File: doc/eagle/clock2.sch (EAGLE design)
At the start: 27 parts, among them J1 LCD 1602, J2 LM35, J3 ds1302 module

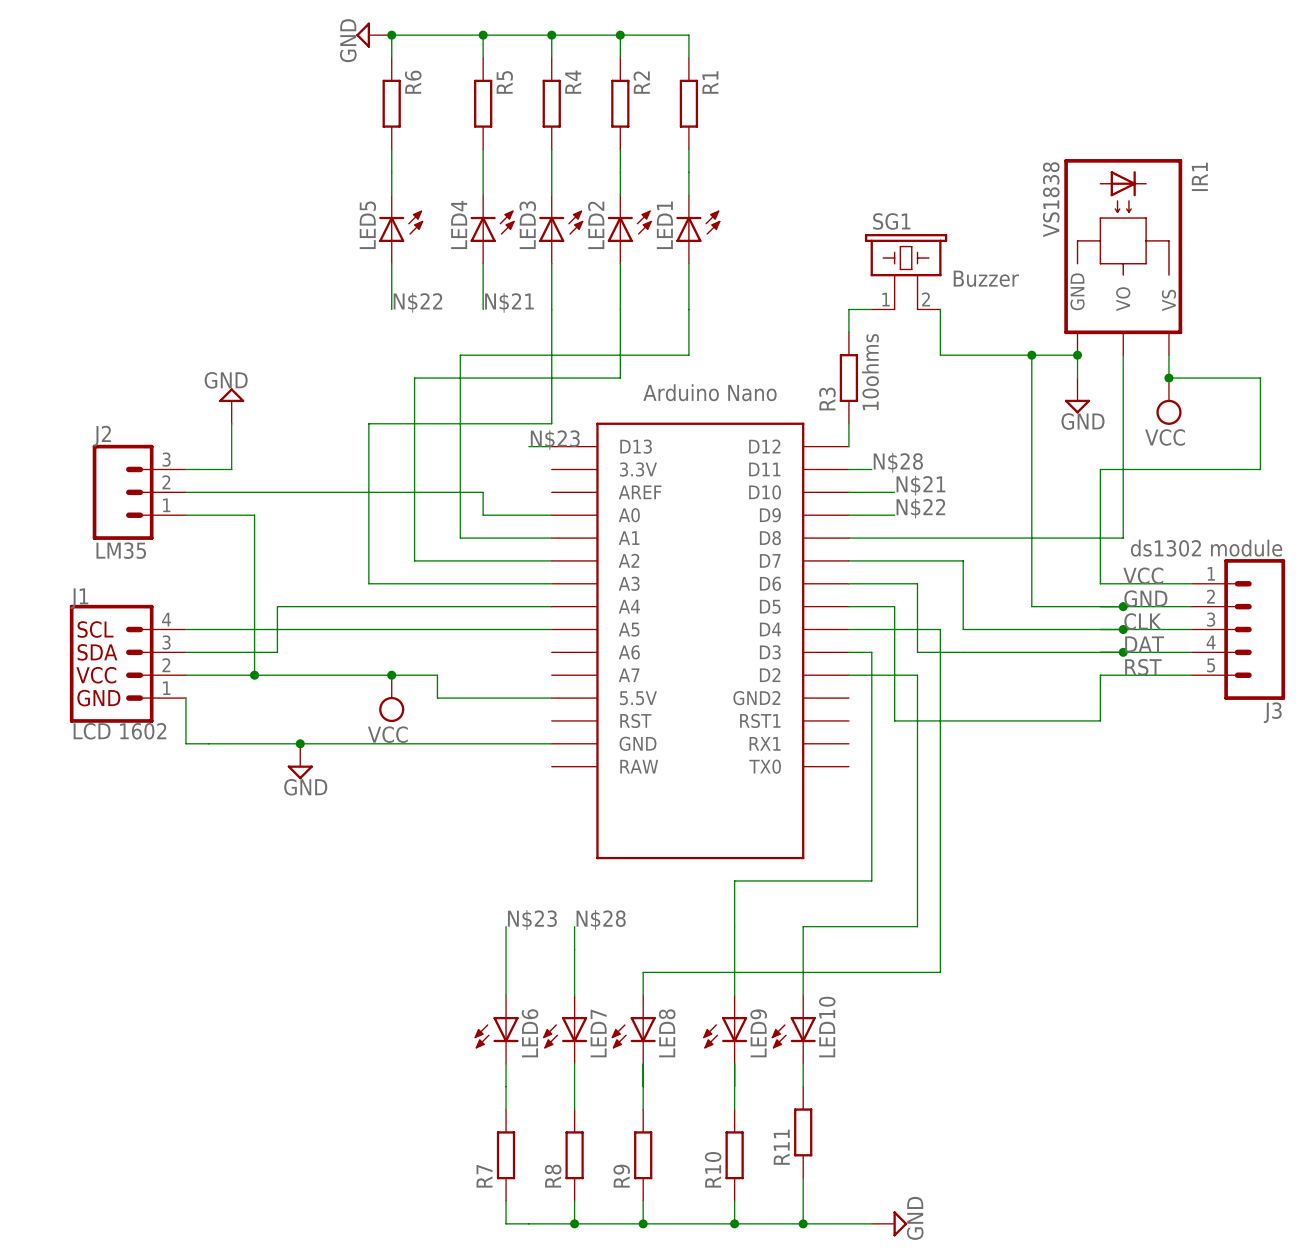
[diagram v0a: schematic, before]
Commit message: changeing sch from fritz to eagle
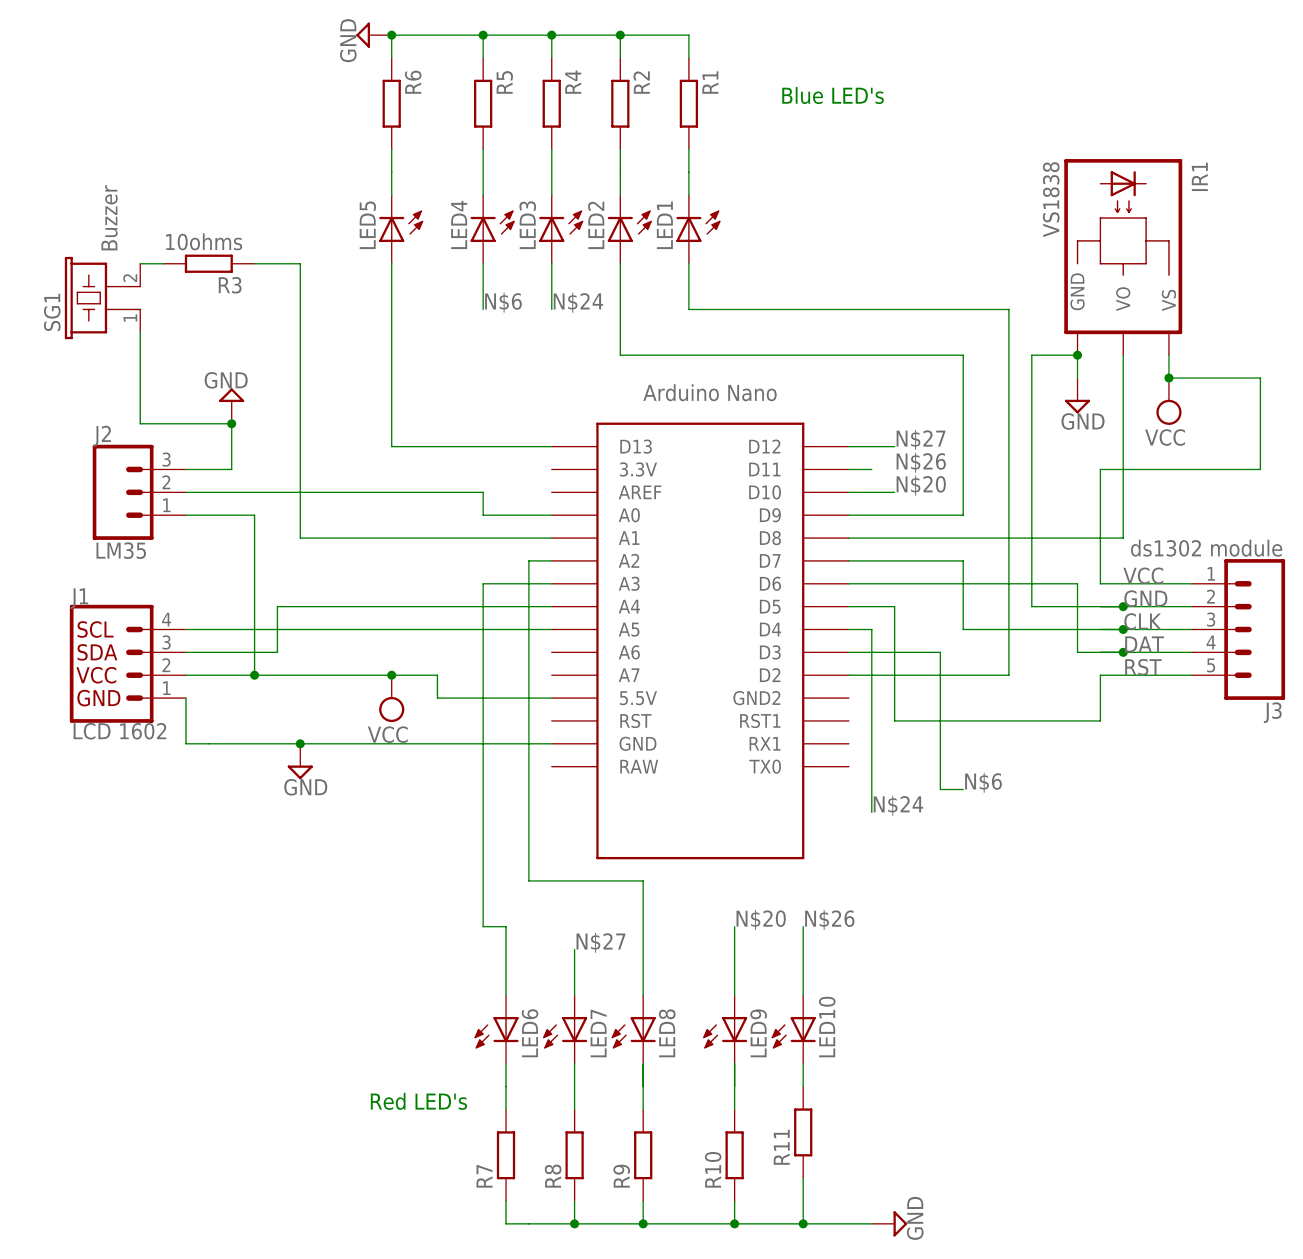
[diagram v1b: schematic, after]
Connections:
- removed net N$25: LED9.A, U$1.D3
- new net N$24: LED3.A, U$1.D4
- new net N$29: LED2.A, U$1.D9
- net DAT: now also U$1.D6
- net GND: now also SG1.1; no longer SG1.2
- net N$1: now also R3.1, U$1.A1; no longer R3.2, SG1.1
- net N$18: now also U$1.A2; no longer U$1.D4
- net N$19: now also LED1.A, U$1.D2; no longer LED2.A, U$1.A2
- net N$2: now also R3.2, SG1.2; no longer R3.1, U$1.D12
- net N$20: now also LED9.A; no longer LED3.A, U$1.A3
- net N$21: no longer LED4.A
- net N$22: now also U$1.D13; no longer U$1.D9
- net N$23: now also U$1.A3; no longer U$1.D13
- net N$26: no longer U$1.D2
- net N$27: now also LED7.A, U$1.D12; no longer U$1.D6
- net N$28: no longer LED7.A
- net N$6: now also LED4.A, U$1.D3; no longer LED1.A, U$1.A1
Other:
- note added: "Blue LED's"
- note added: "Red LED's"
- moved on the sheet: R3, SG1

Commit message: adding remote control code information
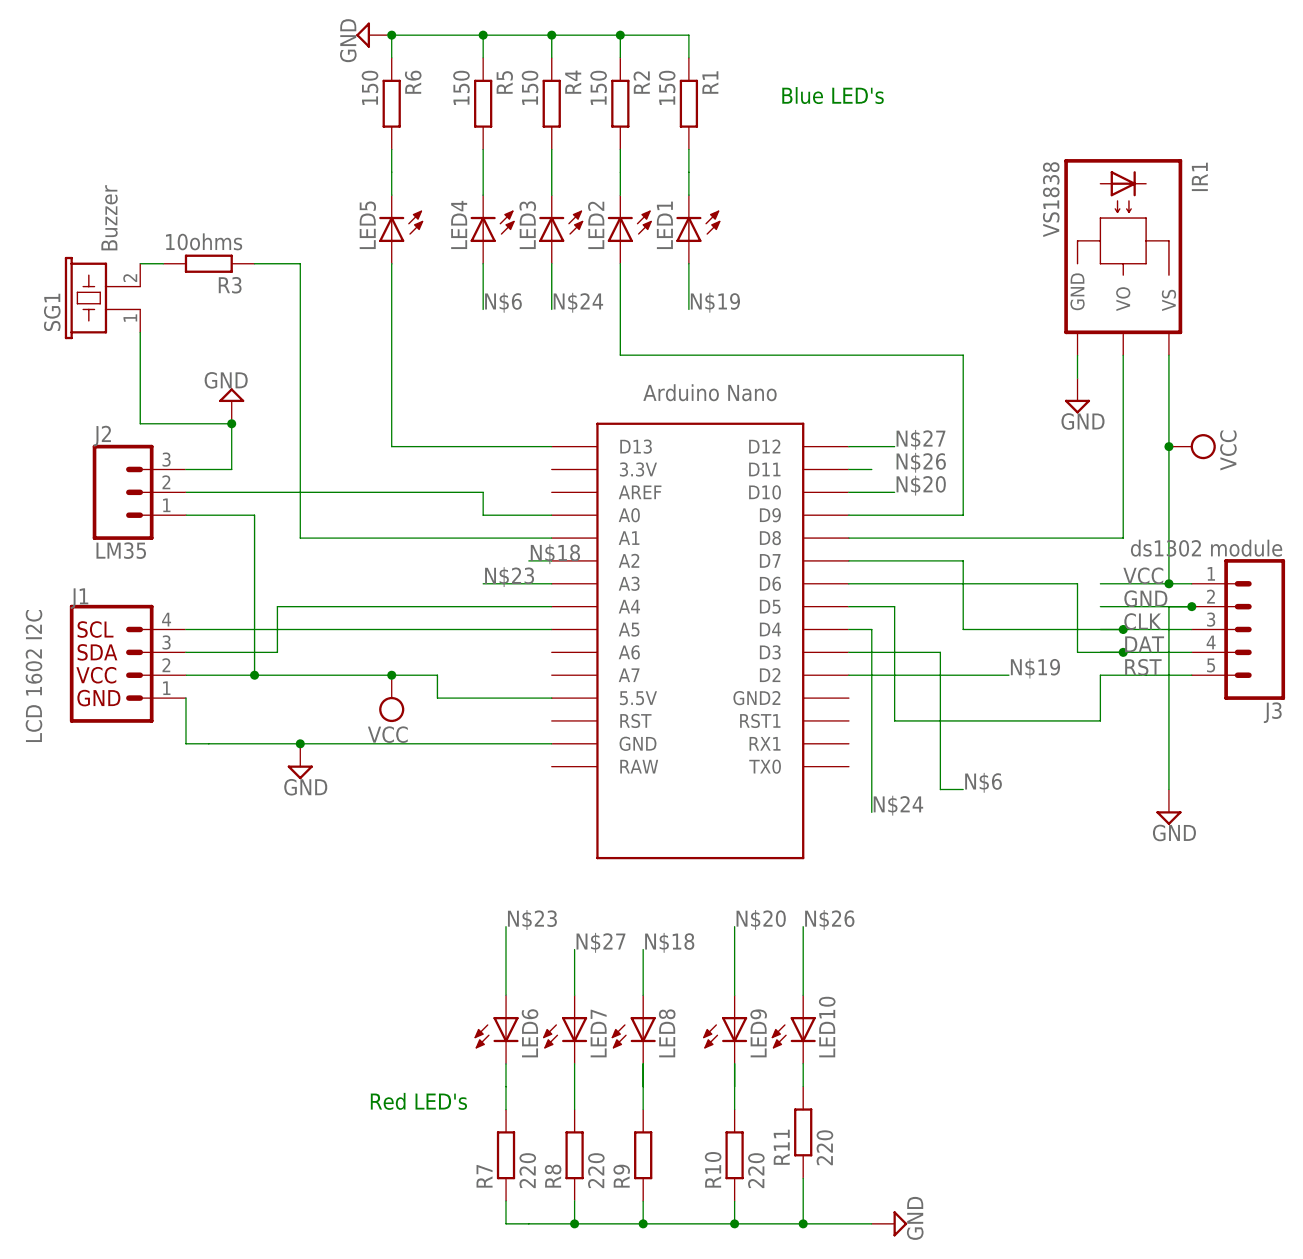
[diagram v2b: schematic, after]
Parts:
- J1: value LCD 1602 -> LCD 1602 I2C
- R1, R2, R4, R5, R6: value (none) -> 150
- R10, R11, R7, R8: value (none) -> 220
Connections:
- new net N$25: U$1.A2
- new net N$30: U$1.A3
- new net N$31: LED1.A
- net N$18: no longer U$1.A2
- net N$19: no longer LED1.A
- net N$23: no longer U$1.A3
